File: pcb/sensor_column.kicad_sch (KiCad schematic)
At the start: 2 parts, among them U210 CD74HC4067SM96

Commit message: pcb: specify component's LCSC part number
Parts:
- C210: LCSC Part # (none) -> C1591
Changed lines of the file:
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@@
+			)
+		)
+		(property "LCSC Part #" "C1591"
+			(at 107.95 40.64 0)
+			(effects
+				(font
+					(size 1.27 1.27)
+				)
+				(hide yes)
 			)
 		)

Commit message: pcb: match component footprint with their actual size
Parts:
- C210: LCSC Part # C1591 -> C160831
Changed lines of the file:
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@@
 			)
 		)
-		(property "LCSC Part #" "C1591"
+		(property "LCSC Part #" "C160831"
 			(at 107.95 40.64 0)
 			(effects

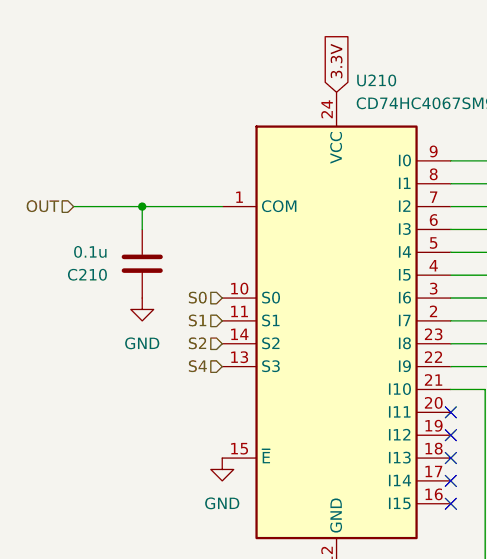
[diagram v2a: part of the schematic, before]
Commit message: pcb: use cheaper hall effect sensor and remove unnecessary capacitor and resistor connected to each sensor
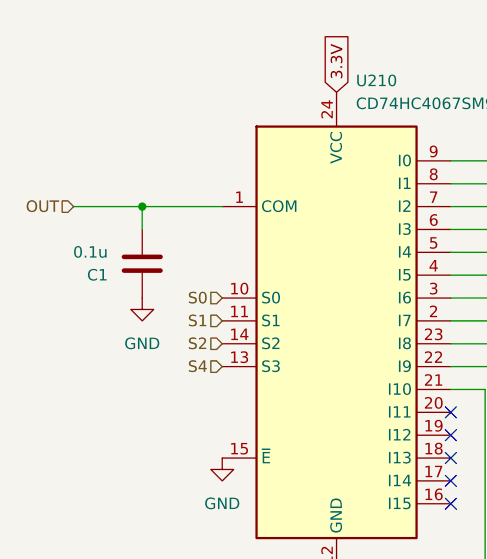
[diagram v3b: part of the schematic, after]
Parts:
- renumbered C210 to C1
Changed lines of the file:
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@@
 		(on_board yes)
 		(dnp no)
-		(property "Reference" "C210"
+		(property "Reference" "C1"
 			(at 104.14 41.9101 0)
 			(effects
@@
 			(project "pompyboard"
 				(path "/e5830f2e-b6bc-440e-bdf9-7651ab21e3a0/026cd3d2-ee49-4aa8-a6be-1ded8cec01b6"
-					(reference "C217")
+					(reference "C8")
 					(unit 1)
 				)
 				(path "/e5830f2e-b6bc-440e-bdf9-7651ab21e3a0/199d6db0-4201-4cdd-9fb1-82dea6ba15a4"
-					(reference "C215")
+					(reference "C6")
 					(unit 1)
 				)
 				(path "/e5830f2e-b6bc-440e-bdf9-7651ab21e3a0/1e9b9d03-fd28-4128-b065-c69f49efdc78"
-					(reference "C216")
+					(reference "C7")
 					(unit 1)
 				)
 				(path "/e5830f2e-b6bc-440e-bdf9-7651ab21e3a0/32a6bd95-01f5-4135-9c38-db23c2d07b5b"
-					(reference "C223")
+					(reference "C14")
 					(unit 1)
 				)
 				(path "/e5830f2e-b6bc-440e-bdf9-7651ab21e3a0/337c22cd-c44a-4633-9334-b6d71fe81175"
-					(reference "C218")
+					(reference "C9")
 					(unit 1)
 				)
 				(path "/e5830f2e-b6bc-440e-bdf9-7651ab21e3a0/3545379e-8a56-4cc0-b1cd-1ab95a742a98"
-					(reference "C220")
+					(reference "C11")
 					(unit 1)
 				)
 				(path "/e5830f2e-b6bc-440e-bdf9-7651ab21e3a0/37c05dbe-2573-4442-a09c-64199e530fd0"
-					(reference "C228")
+					(reference "C19")
 					(unit 1)
 				)
 				(path "/e5830f2e-b6bc-440e-bdf9-7651ab21e3a0/3b901f51-f0bc-4942-b393-88eddae2e0fb"
-					(reference "C214")
+					(reference "C5")
 					(unit 1)
 				)
 				(path "/e5830f2e-b6bc-440e-bdf9-7651ab21e3a0/40784eb3-2b54-4b34-8df6-1f3fa1f53a87"
-					(reference "C225")
+					(reference "C16")
 					(unit 1)
 				)
 				(path "/e5830f2e-b6bc-440e-bdf9-7651ab21e3a0/4681251d-eca7-461a-91bc-bdaba01ac76e"
-					(reference "C227")
+					(reference "C18")
 					(unit 1)
 				)
 				(path "/e5830f2e-b6bc-440e-bdf9-7651ab21e3a0/50286a34-f2f1-4644-a6e6-a1533e4b94cb"
-					(reference "C224")
+					(reference "C15")
 					(unit 1)
 				)
 				(path "/e5830f2e-b6bc-440e-bdf9-7651ab21e3a0/50e477be-0e55-4aaa-84b2-7d9c684572af"
-					(reference "C213")
+					(reference "C4")
 					(unit 1)
 				)
 				(path "/e5830f2e-b6bc-440e-bdf9-7651ab21e3a0/5b101357-7322-4fda-a4d3-48f9091ec2c1"
-					(reference "C221")
+					(reference "C12")
 					(unit 1)
 				)
 				(path "/e5830f2e-b6bc-440e-bdf9-7651ab21e3a0/87cf7185-088d-419a-91bb-1bf069870c4c"
-					(reference "C210")
+					(reference "C1")
 					(unit 1)
 				)
 				(path "/e5830f2e-b6bc-440e-bdf9-7651ab21e3a0/98cec319-fa79-4308-9643-76cbe0d21c4b"
-					(reference "C212")
+					(reference "C3")
 					(unit 1)
 				)
 				(path "/e5830f2e-b6bc-440e-bdf9-7651ab21e3a0/9958ff6a-2571-400e-b341-f3d480d503ab"
-					(reference "C219")
+					(reference "C10")
 					(unit 1)
 				)
 				(path "/e5830f2e-b6bc-440e-bdf9-7651ab21e3a0/afe07e8c-a3bd-4530-abaf-689610bb4fc1"
-					(reference "C211")
+					(reference "C2")
 					(unit 1)
 				)
 				(path "/e5830f2e-b6bc-440e-bdf9-7651ab21e3a0/ba38ac3b-2a26-4096-a08a-23e633321ac9"
-					(reference "C226")
+					(reference "C17")
 					(unit 1)
 				)
 				(path "/e5830f2e-b6bc-440e-bdf9-7651ab21e3a0/c87b1fe2-43d8-4cc7-b93e-7a2d84539e65"
-					(reference "C222")
+					(reference "C13")
 					(unit 1)
 				)

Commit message: pcb: use component from jlcpcb "basic" part instead of "extended" (reduce cost from $242.46 to $222.80)
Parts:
- C1: footprint Capacitor_SMD:C_0201_0603Metric -> Capacitor_SMD:C_0402_1005Metric; LCSC Part # C160831 -> C1525
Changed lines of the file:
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@@
 			)
 		)
-		(property "Footprint" "Capacitor_SMD:C_0201_0603Metric"
+		(property "Footprint" "Capacitor_SMD:C_0402_1005Metric"
 			(at 106.9848 36.83 0)
 			(effects
@@
 			)
 		)
-		(property "LCSC Part #" "C160831"
+		(property "LCSC Part #" "C1525"
 			(at 107.95 40.64 0)
 			(effects

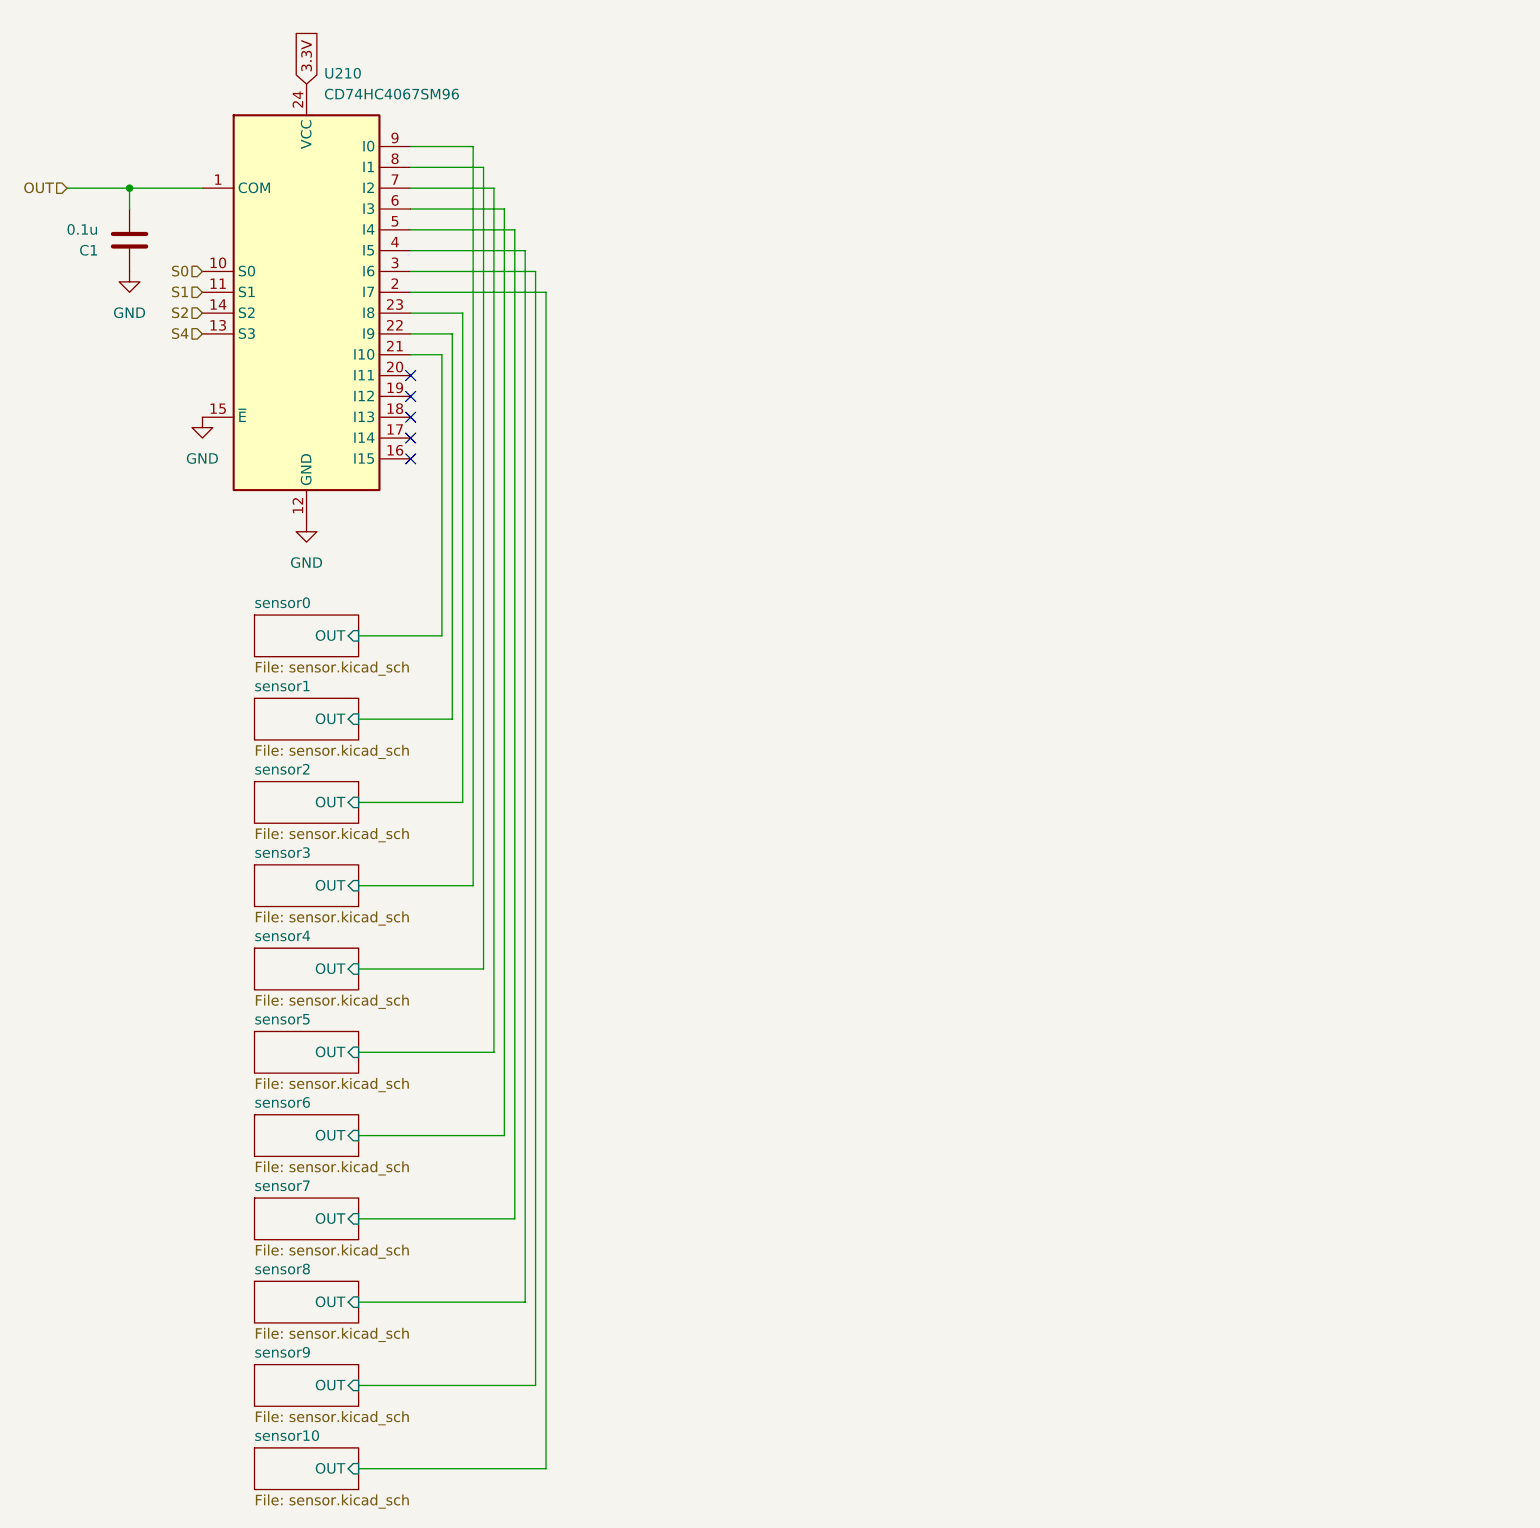
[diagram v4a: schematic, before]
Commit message: pcb: add resistors to reduce multiplexer channel crosstalk
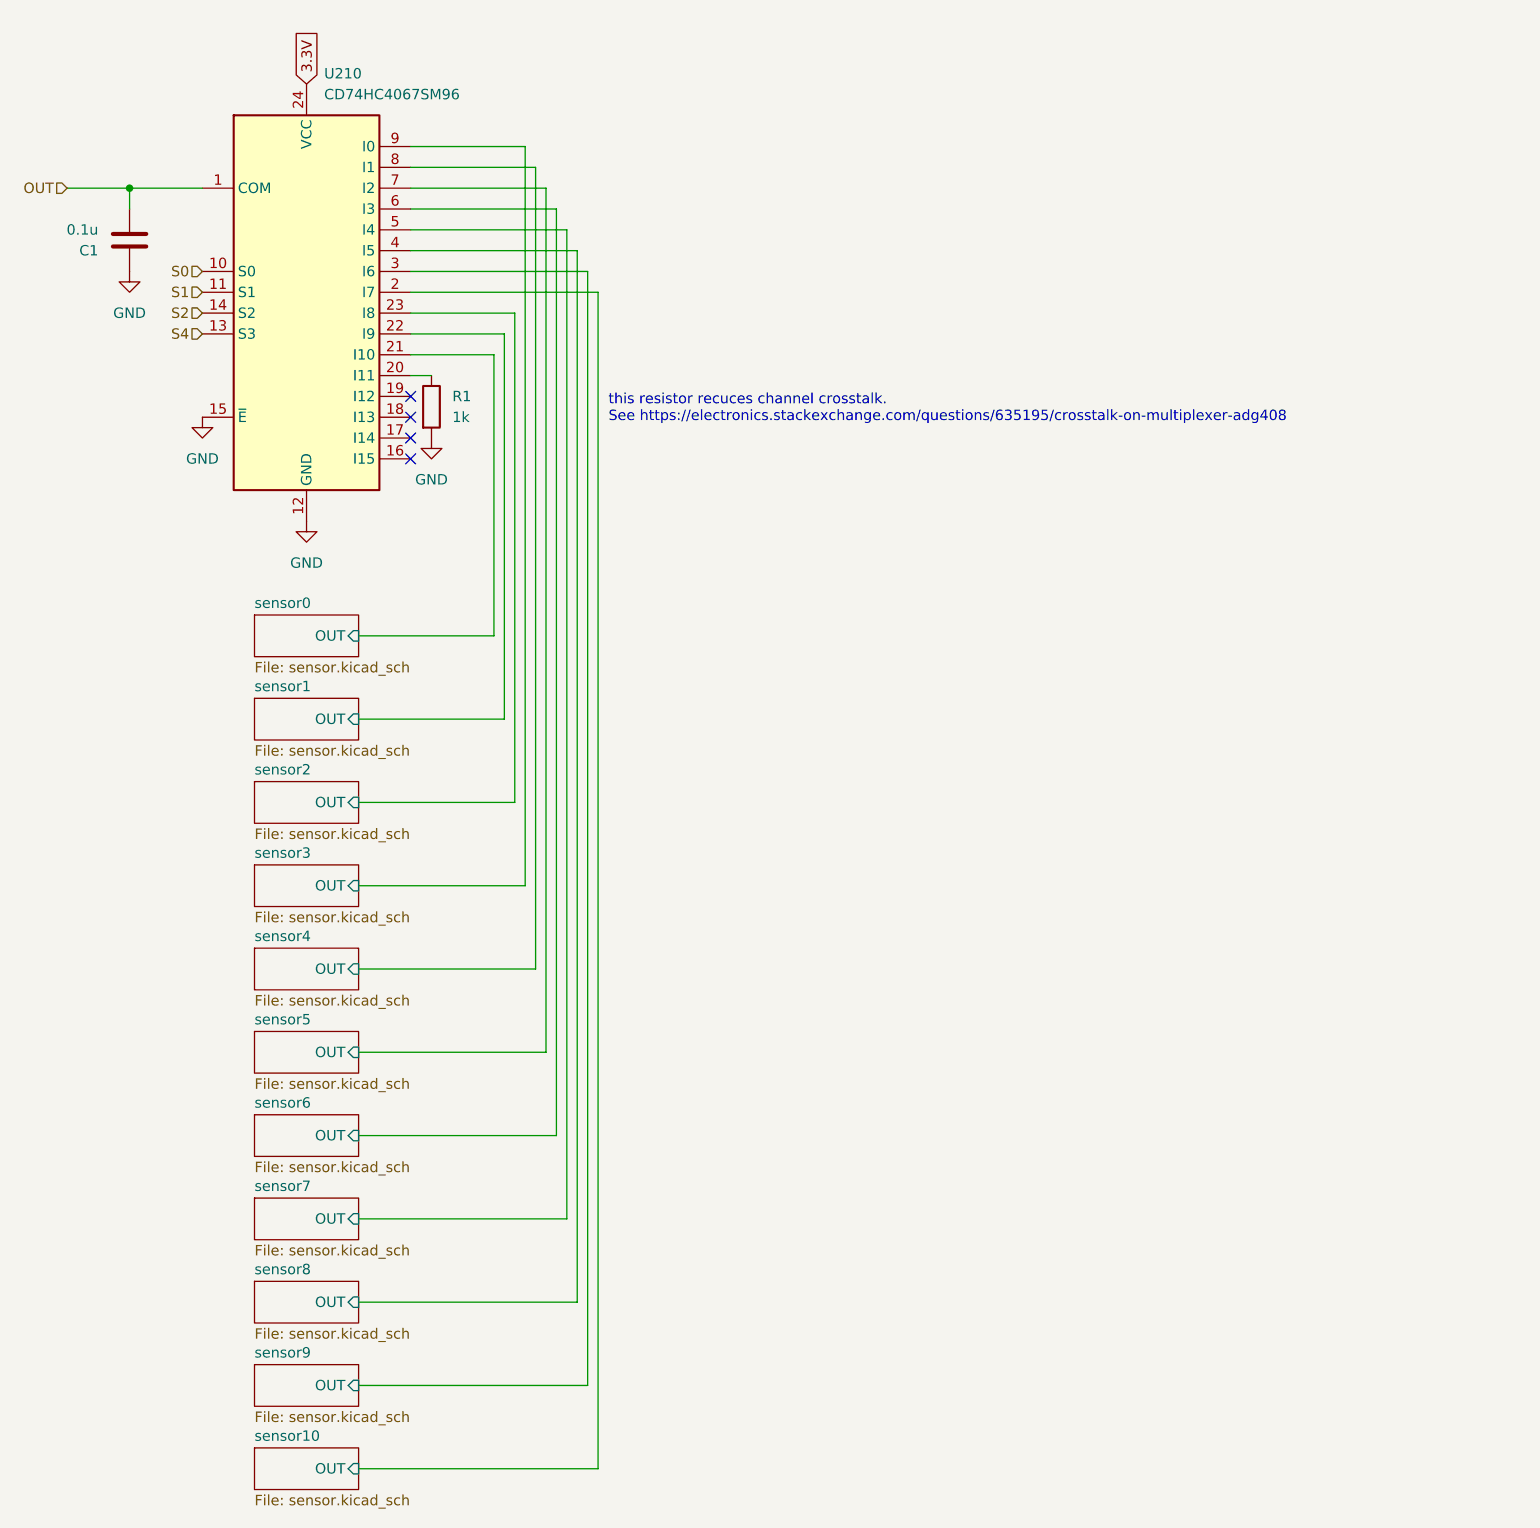
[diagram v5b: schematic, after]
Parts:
- added R1: 1k, Resistor_SMD:R_0402_1005Metric, symbol Device:R
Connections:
- net GND: now also R1.2
- net at U210.20 (I11): now also R1.1
- no-connect marks 5 -> 4
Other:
- note added: "this resistor recuces channel crosstalk. See https://electronics.stackexchange.com/questions/635195/crosstalk-on-multiplexer-adg408"
